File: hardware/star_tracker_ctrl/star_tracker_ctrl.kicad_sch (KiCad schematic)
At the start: 72 parts, among them J1 12V IN, J10 I2C EXP, J11 SPARE IO, J2 CAM USB-A, J20 ESP32 L, J21 ESP32 R, J3 CAM 5V, J30 TMC2209 L, J31 TMC2209 R, J4 MOTOR, J5 DIAG, J6 DS3231, J7 AS5600, J8 HOME, J9 GPS, Q1 IRF4905, Q2 IRF4905, Q3 2N3904, Q4 2N3906, Q5 2N3904, SW1 CONFIG, U2 LM2596T-5.0

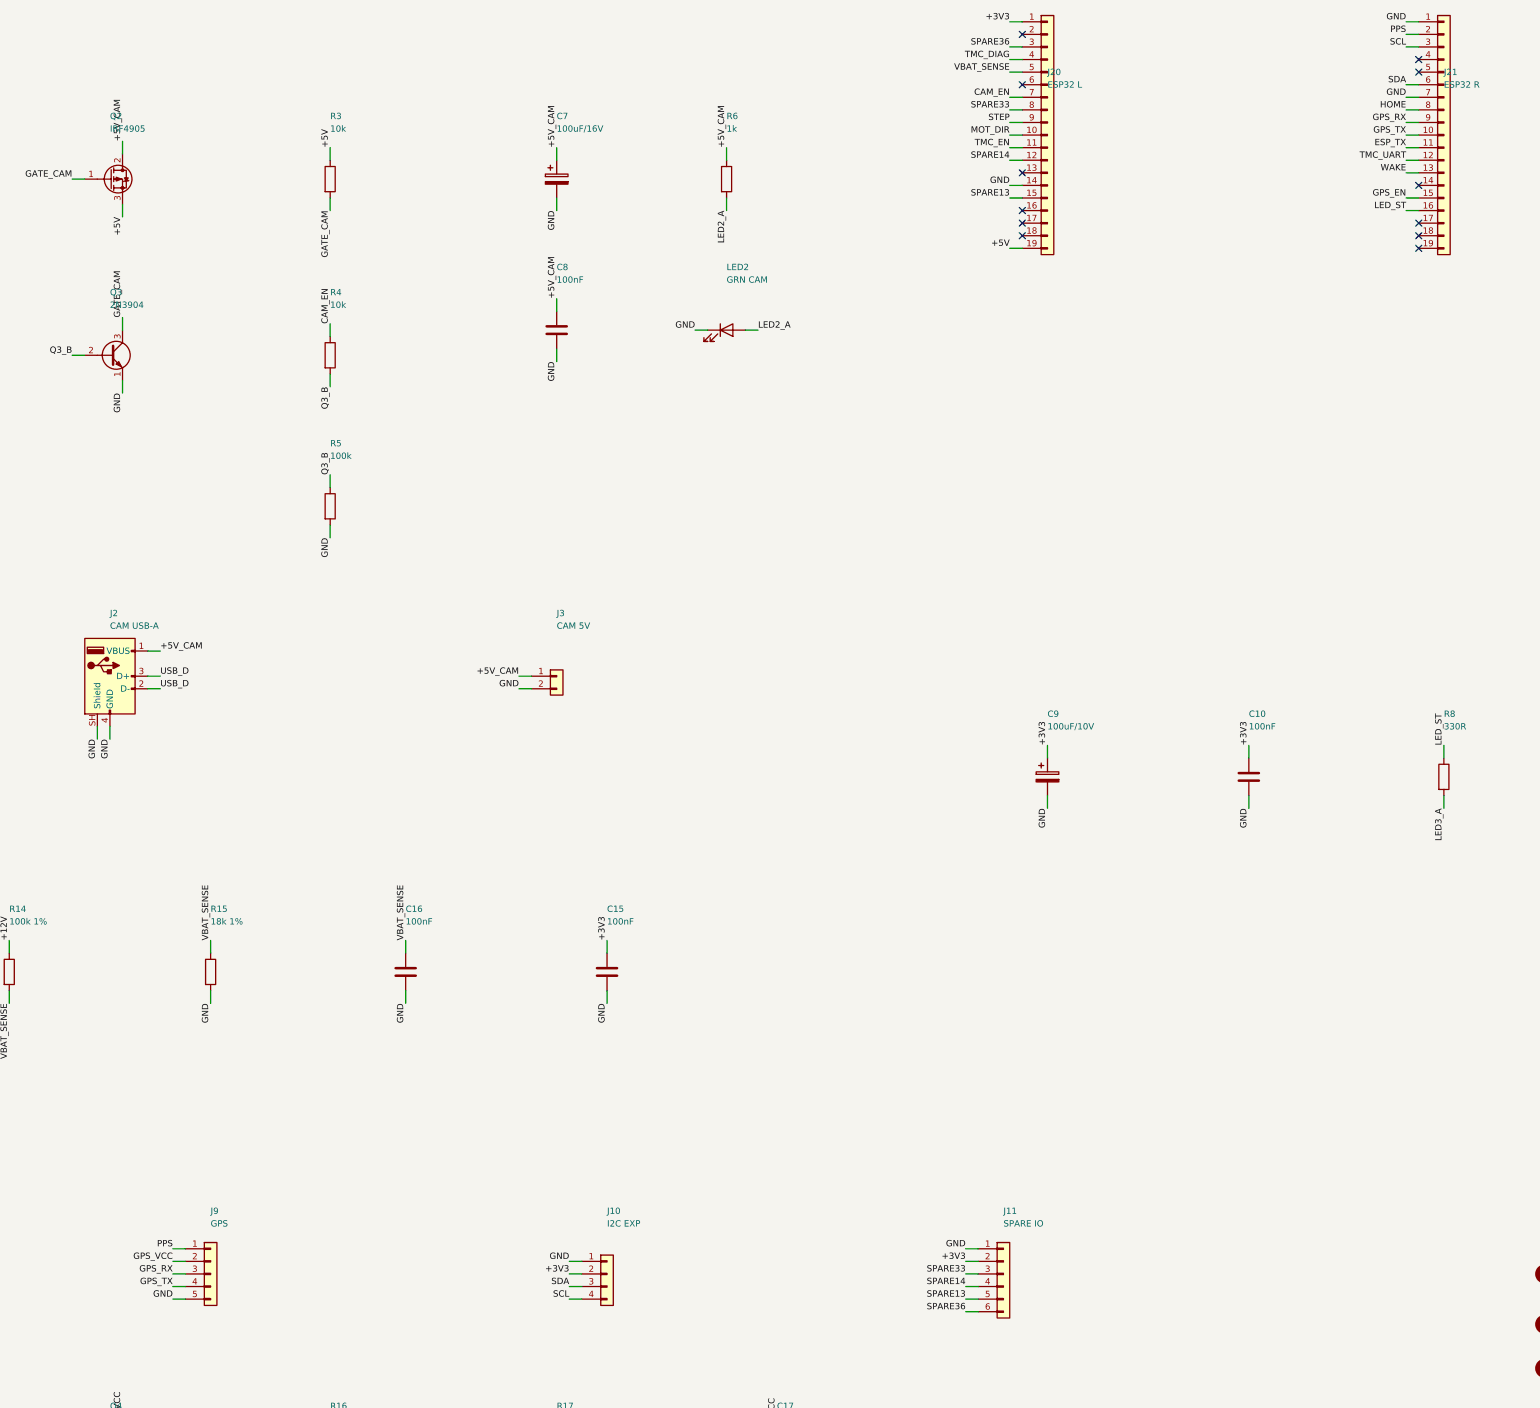
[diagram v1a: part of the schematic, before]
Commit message: Controller board Rev C for the 30-pin ideaspark ESP32
Pin check (firmware/pincheck, 2026-09-27): ESP32-D0WD-V3, 4 MB, no PSRAM;
the on-board OLED answers at 0x3C on GPIO 21/22, so it shares the sensor
bus and GPIO 4 stays free for WAKE.

design.py: the 30-pin map (15 per side, rows 27.94 mm). Upper row serves
the driver, camera switch, divider and status LED; lower row the bottom
connector strip. Changes from Rev B: TMC UART 33/14, DIAG 36, LED_ST 13,
GPS_EN 17 (GPIO 2 left free for download mode), J11 now 4 pins (39, 35).
GPS UART nets named by direction. REV = "C".

route.py: vias keep the fab's hole-to-hole minimum from every pad and via
whatever the net (a GND via sat 0.19 mm from a GND pad's hole); the GND
stitch runs twice; GND_RESCUE pads get an escape before any signal is
routed -- the bottom strip's four GND end pins, which signal tracks fenced
in on both layers.

Result: fully routed, ERC 0, DRC 0 unconnected / clearance / hole-to-hole;
only cosmetic silkscreen overlaps. Board render and schematic PDF
regenerated. FIRMWARE.md, PCB.md, HARDWARE.md, RESUME.md and README follow;
the assembly guide, its Fritzing views and PDF are rebuilt from the new
layout. KiCad lock files ignored.

Co-Authored-By: Claude Opus 5.5 <noreply@anthropic.com>
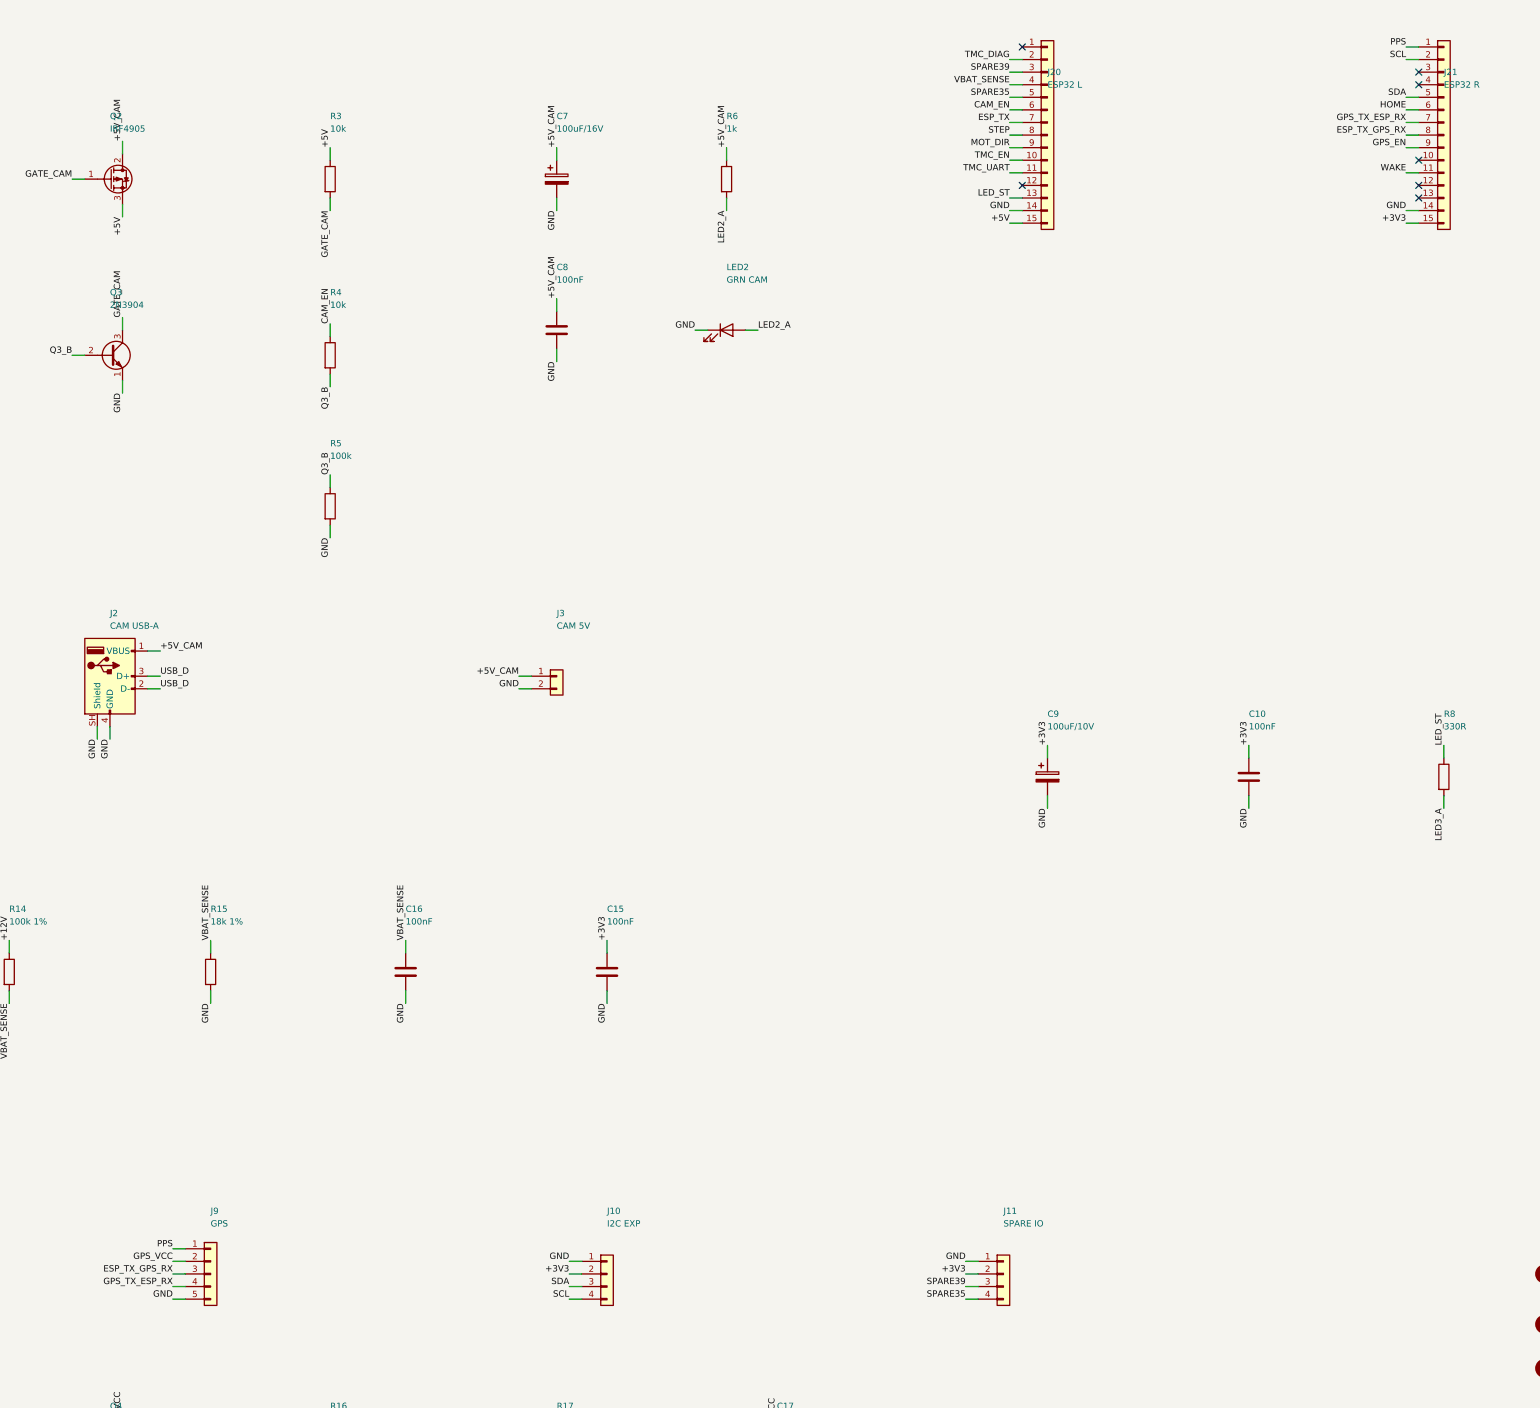
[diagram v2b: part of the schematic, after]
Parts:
- removed J11: SPARE IO, Connector_PinHeader_2.54mm:PinHeader_1x06_P2.54mm_Vertical, symbol Connector_Generic:Conn_01x06
- removed J20: ESP32 L, Connector_PinSocket_2.54mm:PinSocket_1x19_P2.54mm_Vertical, symbol Connector_Generic:Conn_01x19
- removed J21: ESP32 R, Connector_PinSocket_2.54mm:PinSocket_1x19_P2.54mm_Vertical, symbol Connector_Generic:Conn_01x19
- added J11: SPARE IO, Connector_PinHeader_2.54mm:PinHeader_1x04_P2.54mm_Vertical, symbol Connector_Generic:Conn_01x04
- added J20: ESP32 L, Connector_PinSocket_2.54mm:PinSocket_1x15_P2.54mm_Vertical, symbol Connector_Generic:Conn_01x15
- added J21: ESP32 R, Connector_PinSocket_2.54mm:PinSocket_1x15_P2.54mm_Vertical, symbol Connector_Generic:Conn_01x15
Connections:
- net +3V3: now also J11.2 (Pin_2), J21.15 (Pin_15)
- net +5V: now also J20.15 (Pin_15)
- net CAM_EN: now also J20.6 (Pin_6)
- net ESP_TX: now also J20.7 (Pin_7)
- net GND: now also J11.1 (Pin_1), J20.14 (Pin_14), J21.14 (Pin_14)
- net GPS_EN: now also J21.9 (Pin_9)
- net HOME: now also J21.6 (Pin_6)
- net LED_ST: now also J20.13 (Pin_13)
- net MOT_DIR: now also J20.9 (Pin_9)
- net PPS: now also J21.1 (Pin_1)
- net SCL: now also J21.2 (Pin_2)
- net SDA: now also J21.5 (Pin_5)
- net STEP: now also J20.8 (Pin_8)
- net TMC_DIAG: now also J20.2 (Pin_2)
- net TMC_EN: now also J20.10 (Pin_10)
- net TMC_UART: now also J20.11 (Pin_11)
- net VBAT_SENSE: now also J20.4 (Pin_4)
- net WAKE: now also J21.11 (Pin_11)
- net GPS_RX renamed ESP_TX_GPS_RX
- net ESP_TX_GPS_RX: now also J21.8 (Pin_8)
- net GPS_TX renamed GPS_TX_ESP_RX
- net GPS_TX_ESP_RX: now also J21.7 (Pin_7)
- new net SPARE35: J11.4 (Pin_4), J20.5 (Pin_5)
- new net SPARE39: J11.3 (Pin_3), J20.3 (Pin_3)
- no-connect marks 14 -> 9
